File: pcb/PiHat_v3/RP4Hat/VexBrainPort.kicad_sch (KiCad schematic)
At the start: 3 parts, among them J1 Conn_01x04, U1 ST3485ECDR

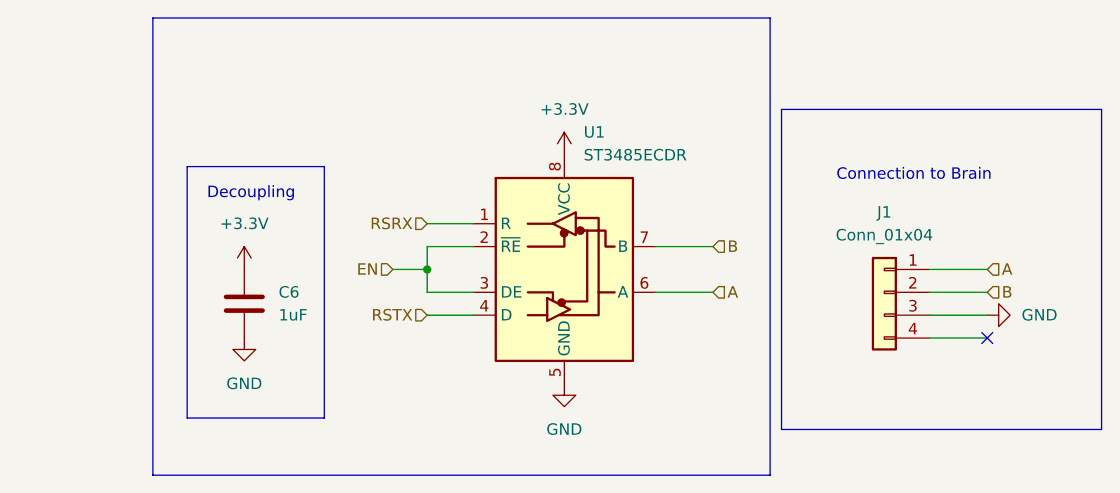
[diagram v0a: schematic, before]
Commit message: move pulldown resistor into sheet
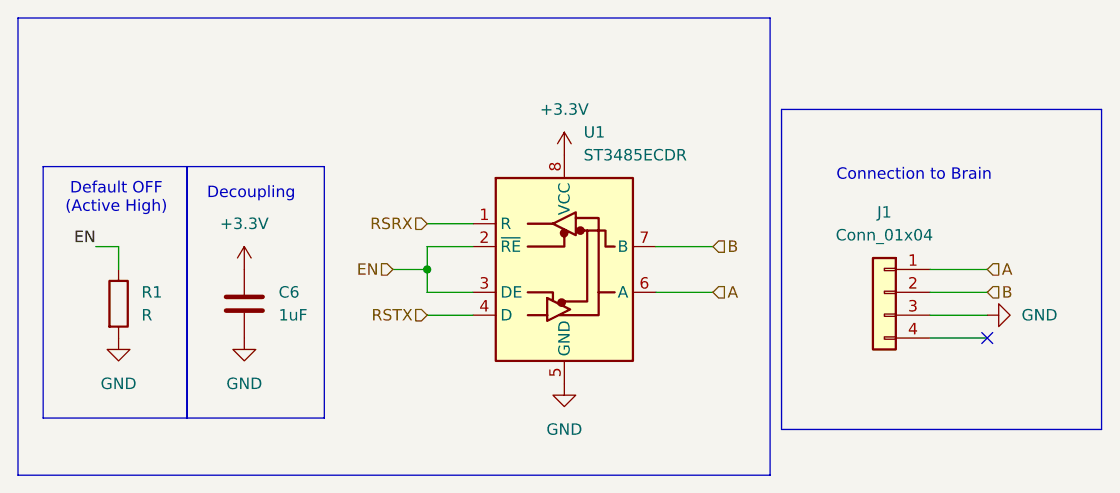
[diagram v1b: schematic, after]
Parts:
- added R1: R, symbol Device:R
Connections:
- net EN: now also R1.1
- net GND: now also R1.2
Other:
- note added: "Default OFF (Active High)"
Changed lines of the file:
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@@
 	(paper "A4")
 	(rectangle
-		(start 81.28 68.58)
+		(start 69.088 85.09)
+		(end 85.09 113.03)
+		(stroke
+			(width 0)
+			(type default)
+		)
+		(fill
+			(type none)
+		)
+	)
+	(rectangle
+		(start 66.294 68.58)
 		(end 149.86 119.38)
 		(stroke
@@
 		(exclude_from_sim no)
 		(at 165.862 86.106 0)
+		(effects
+			(font
+				(size 1.27 1.27)
+			)
+		)
+	)
+	(text "Default OFF \n(Active High)"
+		(exclude_from_sim no)
+		(at 77.216 88.646 0)
 		(effects
 			(font
@@
 	(wire
 		(pts
+			(xy 74.93 93.98) (xy 77.47 93.98)
+		)
+		(stroke
+			(width 0)
+			(type default)
+		)
+	)
+	(wire
+		(pts
 			(xy 111.76 99.06) (xy 116.84 99.06)
 		)
@@
 	(wire
 		(pts
+			(xy 77.47 93.98) (xy 77.47 96.52)
+		)
+		(stroke
+			(width 0)
+			(type default)
+		)
+	)
+	(wire
+		(pts
 			(xy 107.95 96.52) (xy 111.76 96.52)
 		)
@@
 			(width 0)
 			(type default)
+		)
+	)
+	(label "EN"
+		(at 74.93 93.98 180)
+		(effects
+			(font
+				(size 1.27 1.27)
+			)
+			(justify right bottom)
 		)
 	)
@@
 	)
 	(symbol
+		(lib_id "Device:R")
+		(at 77.47 100.33 0)
+		(unit 1)
+		(body_style 1)
+		(exclude_from_sim no)
+		(in_bom yes)
+		(on_board yes)
+		(in_pos_files yes)
+		(dnp no)
+		(fields_autoplaced yes)
+		(property "Reference" "R1"
+			(at 80.01 99.0599 0)
+			(show_name no)
+			(do_not_autoplace no)
+			(effects
+				(font
+					(size 1.27 1.27)
+				)
+				(justify left)
+			)
+		)
+		(property "Value" "R"
+			(at 80.01 101.5999 0)
+			(show_name no)
+			(do_not_autoplace no)
+			(effects
+				(font
+					(size 1.27 1.27)
+				)
+				(justify left)
+			)
+		)
+		(property "Footprint" ""
+			(at 75.692 100.33 90)
+			(hide yes)
+			(show_name no)
+			(do_not_autoplace no)
+			(effects
+				(font
+					(size 1.27 1.27)
+				)
+			)
+		)
+		(property "Datasheet" ""
+			(at 77.47 100.33 0)
+			(hide yes)
+			(show_name no)
+			(do_not_autoplace no)
+			(effects
+				(font
+					(size 1.27 1.27)
+				)
+			)
+		)
+		(property "Description" "Resistor"
+			(at 77.47 100.33 0)
+			(hide yes)
+			(show_name no)
+			(do_not_autoplace no)
+			(effects
+				(font
+					(size 1.27 1.27)
+				)
+			)
+		)
+		(pin "2"
+		)
+		(pin "1"
+		)
+		(instances
+			(project "RP4Hat"
+				(path "/48e8712f-9e83-40b5-843b-6f1e3e03f403/239f7877-3107-47af-b6b0-cc45091d5b60"
+					(reference "R1")
+					(unit 1)
+				)
+			)
+		)
+	)
+	(symbol
 		(lib_id "power:GND")
 		(at 173.99 101.6 90)
@@
 					(unit 1)
 				)
+			)
+		)
+	)
+	(symbol
+		(lib_id "power:GND")
+		(at 77.47 104.14 0)
+		(unit 1)
+		(body_style 1)
+		(exclude_from_sim no)
+		(in_bom yes)
+		(on_board yes)
+		(in_pos_files yes)
+		(dnp no)
+		(fields_autoplaced yes)
+		(property "Reference" "#PWR06"
+			(at 77.47 110.49 0)
+			(hide yes)
+			(show_name no)
+			(do_not_autoplace no)
+			(effects
+				(font
+					(size 1.27 1.27)
+				)
+			)
+		)
+		(property "Value" "GND"
+			(at 77.47 109.22 0)
+			(show_name no)
+			(do_not_autoplace no)
+			(effects
+				(font
+					(size 1.27 1.27)
+				)
+			)
+		)
+		(property "Footprint" ""
+			(at 77.47 104.14 0)
+			(hide yes)
+			(show_name no)
+			(do_not_autoplace no)
+			(effects
+				(font
+					(size 1.27 1.27)
+				)
+			)
+		)
+		(property "Datasheet" ""
+			(at 77.47 104.14 0)
+			(hide yes)
+			(show_name no)
+			(do_not_autoplace no)
+			(effects
+				(font
+					(size 1.27 1.27)
+				)
+			)
+		)
+		(property "Description" "Power symbol creates a global label with name \"GND\" , ground"
+			(at 77.47 104.14 0)
+			(hide yes)
+			(show_name no)
+			(do_not_autoplace no)
+			(effects
+				(font
+					(size 1.27 1.27)
+				)
+			)
+		)
+		(pin "1"
+		)
+		(instances
+			(project "RP4Hat"
+				(path "/48e8712f-9e83-40b5-843b-6f1e3e03f403/239f7877-3107-47af-b6b0-cc45091d5b60"
+					(reference "#PWR06")
+					(unit 1)
+				)

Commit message: big potato shi
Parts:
- R1: value R -> 10k; footprint (none) -> Resistor_SMD:R_0805_2012Metric_Pad1.20x1.40mm_HandSolder
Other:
- note added: "Default Receive"
- note removed: "Default OFF (Active High)"
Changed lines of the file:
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@@
 		)
 	)
-	(text "Default OFF \n(Active High)"
+	(text "Default Receive\n"
 		(exclude_from_sim no)
 		(at 77.216 88.646 0)
@@
 			)
 		)
-		(property "Value" "R"
+		(property "Value" "10k"
 			(at 80.01 101.5999 0)
 			(show_name no)
@@
 			)
 		)
-		(property "Footprint" ""
+		(property "Footprint" "Resistor_SMD:R_0805_2012Metric_Pad1.20x1.40mm_HandSolder"
 			(at 75.692 100.33 90)
 			(hide yes)
